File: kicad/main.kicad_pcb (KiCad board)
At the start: 2 copper layers, 198.1 x 99.1 mm, 64 parts, among them J1 Jack-DC, J12 I2C1, J14 LCD_Conn, J15 VIA_A, J2 UART, J3 Data, J4 PWR, J5 uSD, J7 IO~{EN}_{[5..7]}, J8 Control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

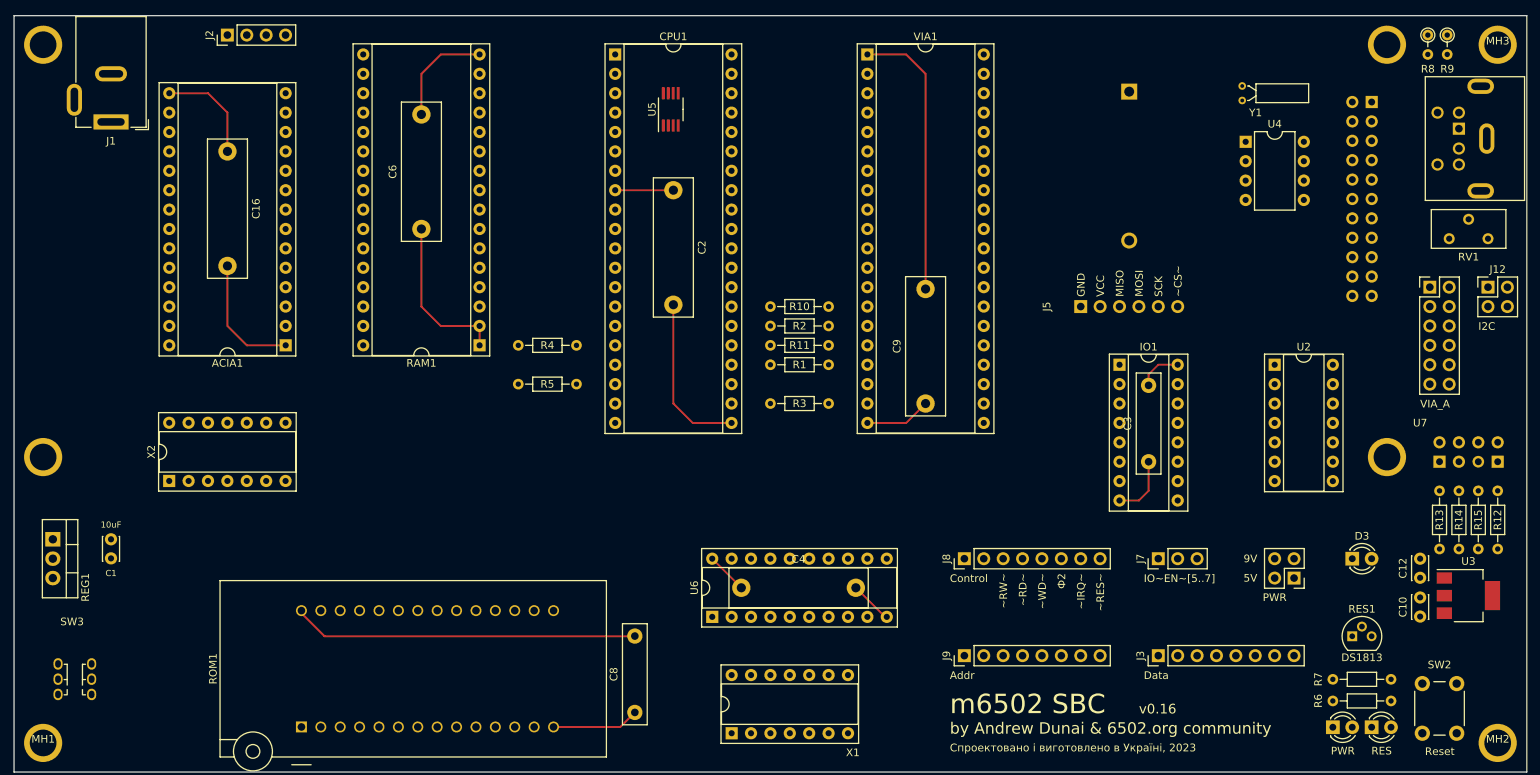
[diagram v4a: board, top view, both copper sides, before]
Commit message: Generate top silk layer with Kicad
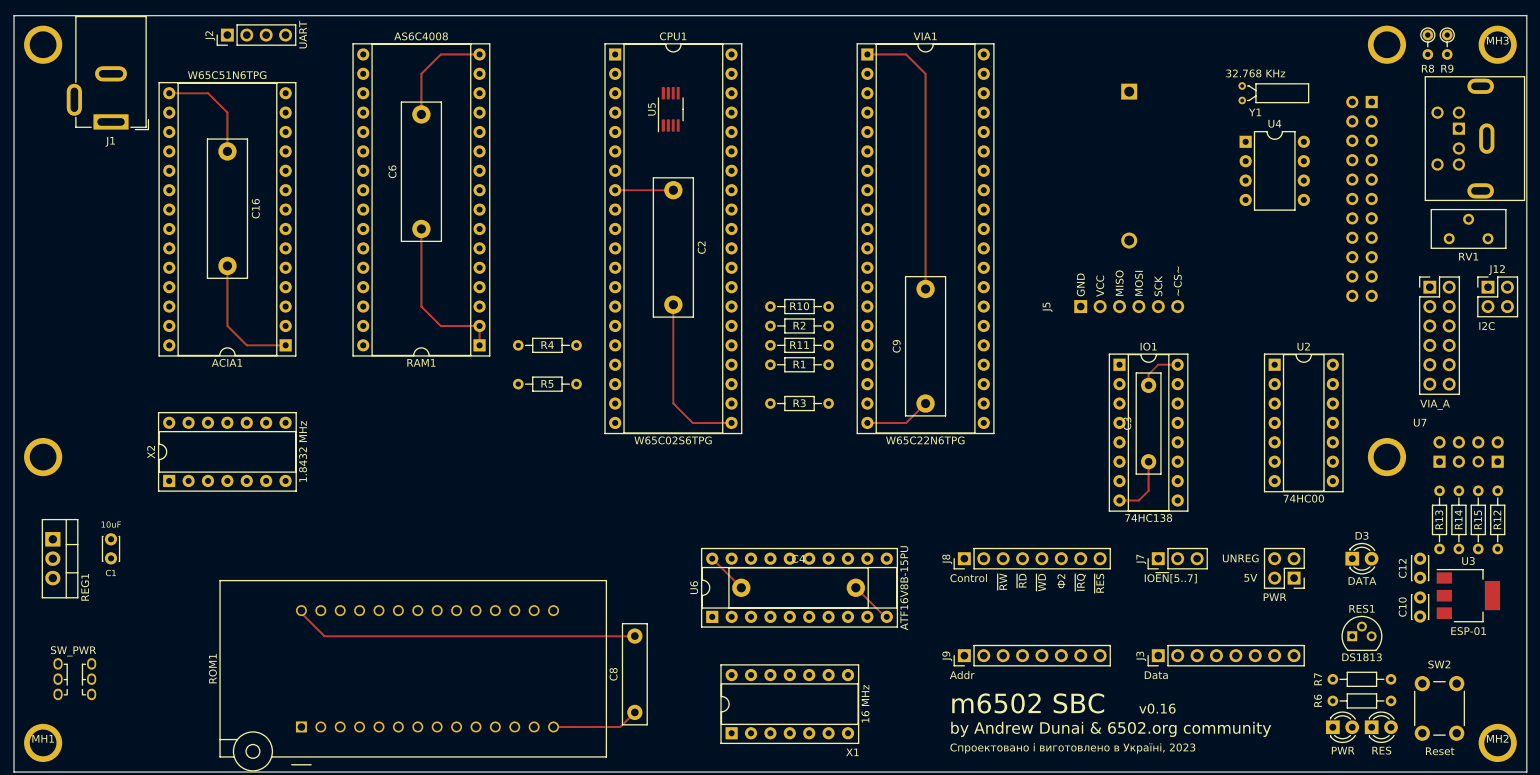
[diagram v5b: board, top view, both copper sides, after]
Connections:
- net +9V renamed +5VA
- net RX renamed ACIARX
- net TX renamed ACIATX
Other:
- board text added: "IO~{EN}[5..7]"
- board text added: "~{IRQ}"
- board text added: "~{RD}"
- board text added: "~{RES}"
- board text added: "~{RW}"
- board text added: "~{WD}"
- board text removed: "IO~EN~[5..7]"
- board text removed: "~IRQ~"
- board text removed: "~RD~"
- board text removed: "~RES~"
- board text removed: "~RW~"
- board text removed: "~WD~"

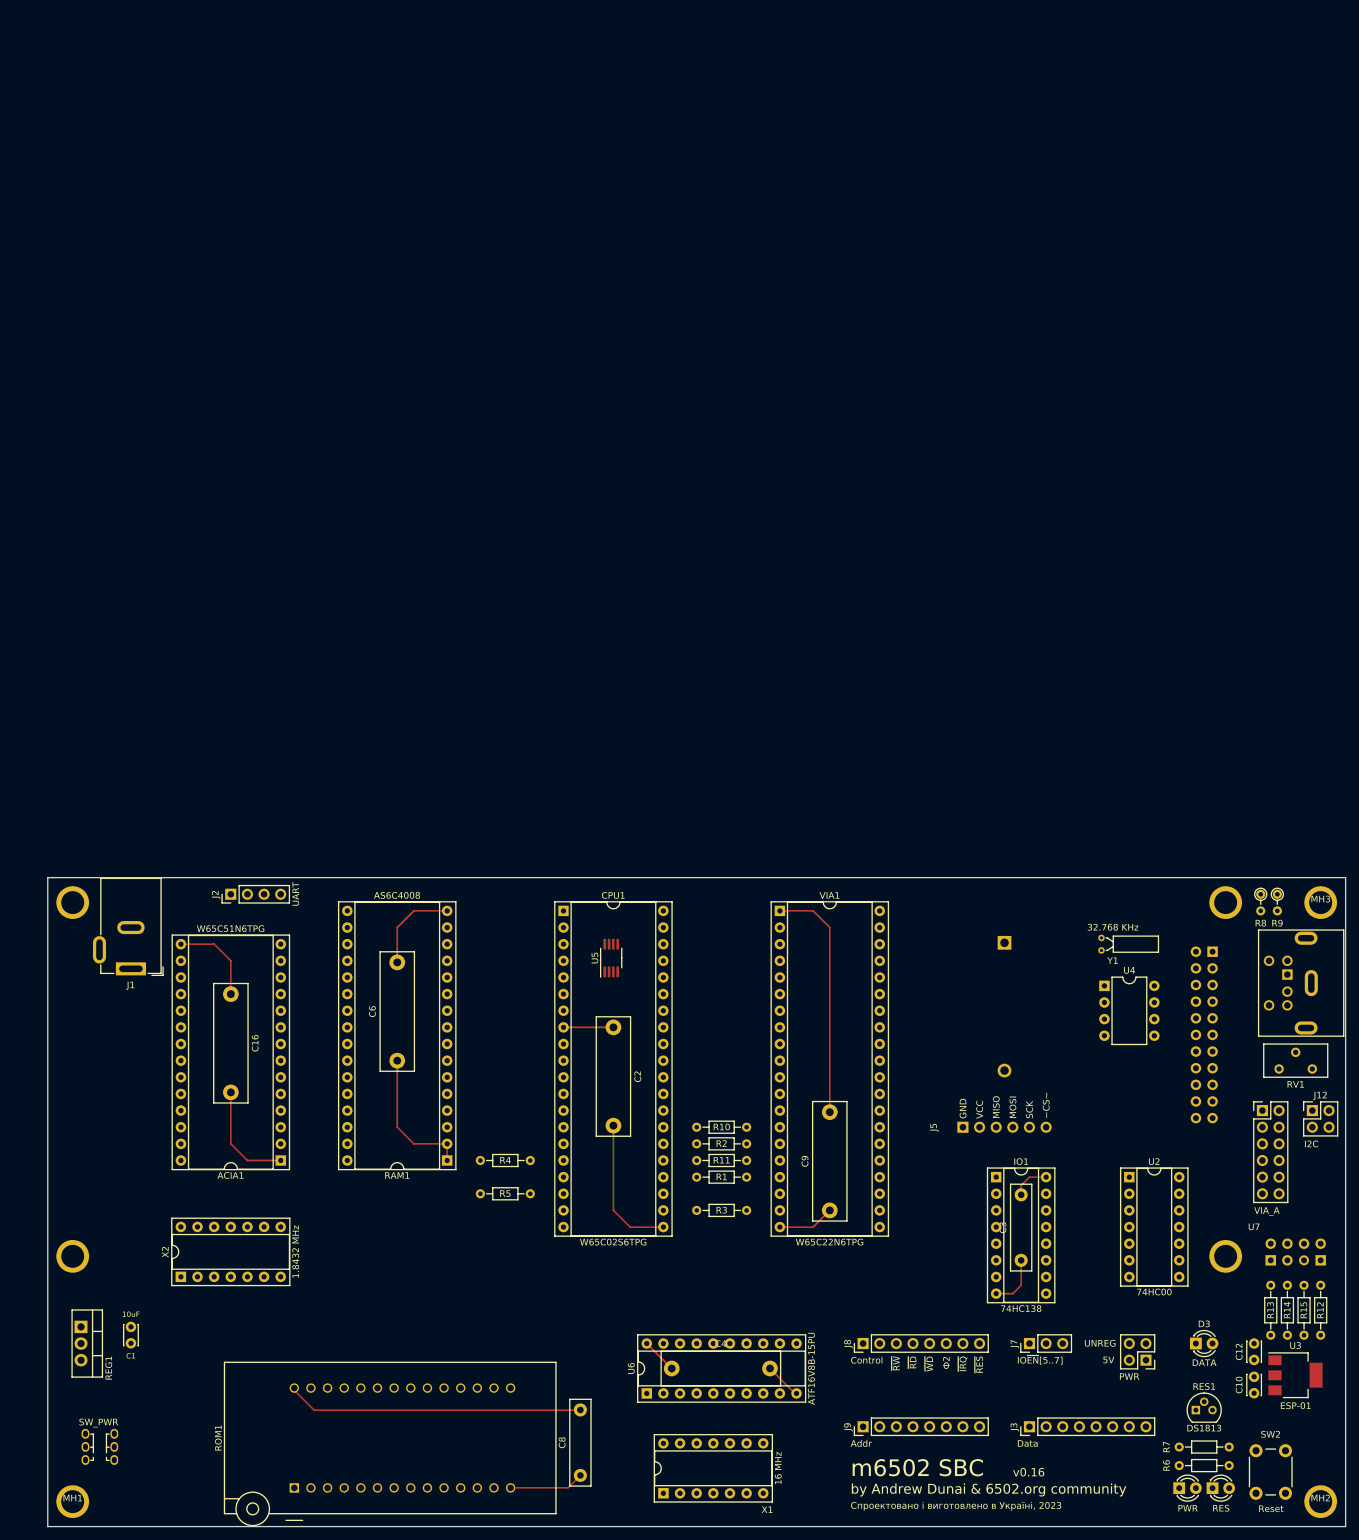
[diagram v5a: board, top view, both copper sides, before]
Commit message: Route /RST to ESP-01
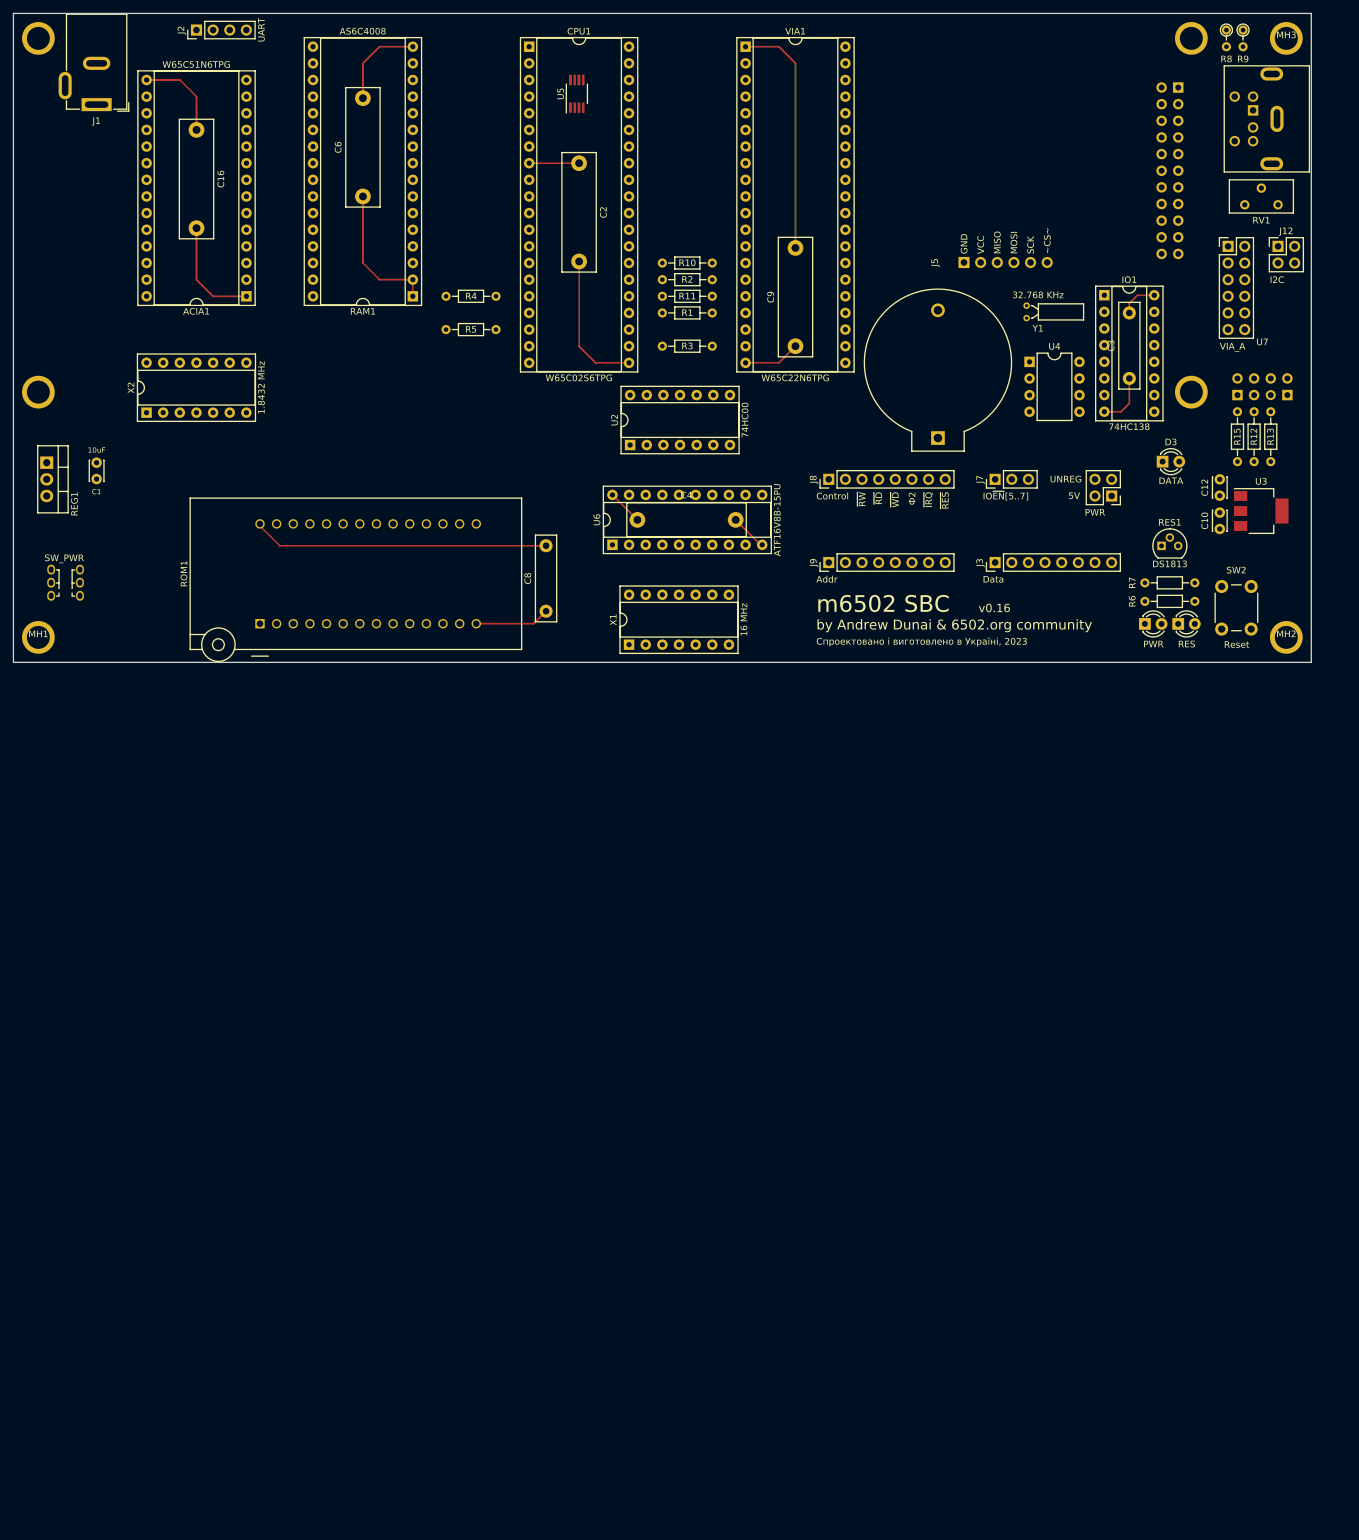
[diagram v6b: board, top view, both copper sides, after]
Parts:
- removed R14: 10K, Resistor_THT:R_Axial_DIN0204_L3.6mm_D1.6mm_P7.62mm_Horizontal
- BT1: moved to F.Cu
- U7: value ESP-01 -> ESP-01-v2
- moved C3 135.6 mm to (180.3, -53.3)
- moved IO1 135.6 mm to (176.5, -66.0)
- moved U2 135.3 mm to (104.1, -43.2), turned to 90 degrees
- moved D3 134.7 mm to (185.4, -40.6)
- moved R12 133.6 mm to (201.9, -40.6)
- moved R13 133.4 mm to (199.4, -48.3)
- moved U7 132.2 mm to (200.7, -54.6)
- moved ACIA1 132.0 mm to (45.6, -65.9)
- moved C10 132.0 mm to (194.2, -30.4)
- moved C12 132.0 mm to (194.2, -35.4)
- moved C16 132.0 mm to (38.0, -91.3)
- moved C2 132.0 mm to (96.3, -86.2)
- moved C6 132.0 mm to (63.4, -81.1)
- moved CPU1 132.0 mm to (88.7, -104.0)
- moved D1 132.0 mm to (182.7, -15.9)
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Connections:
- U7 pad 7: Net-(U7-~{RST}) -> ~{RES}

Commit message: Update silkscreen
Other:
- board text added: "65ad02 SBC"
- board text removed: "m6502 SBC"
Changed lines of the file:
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@@
     (effects (font (size 1 1) (thickness 0.15)) (justify right bottom))
   )
-  (gr_text "m6502 SBC" (at 132.555 -18.89) (layer "F.SilkS")
+  (gr_text "65ad02 SBC" (at 132.555 -18.89) (layer "F.SilkS")
     (effects (font (size 2.54 2.54) (thickness 0.3)) (justify left))
   )

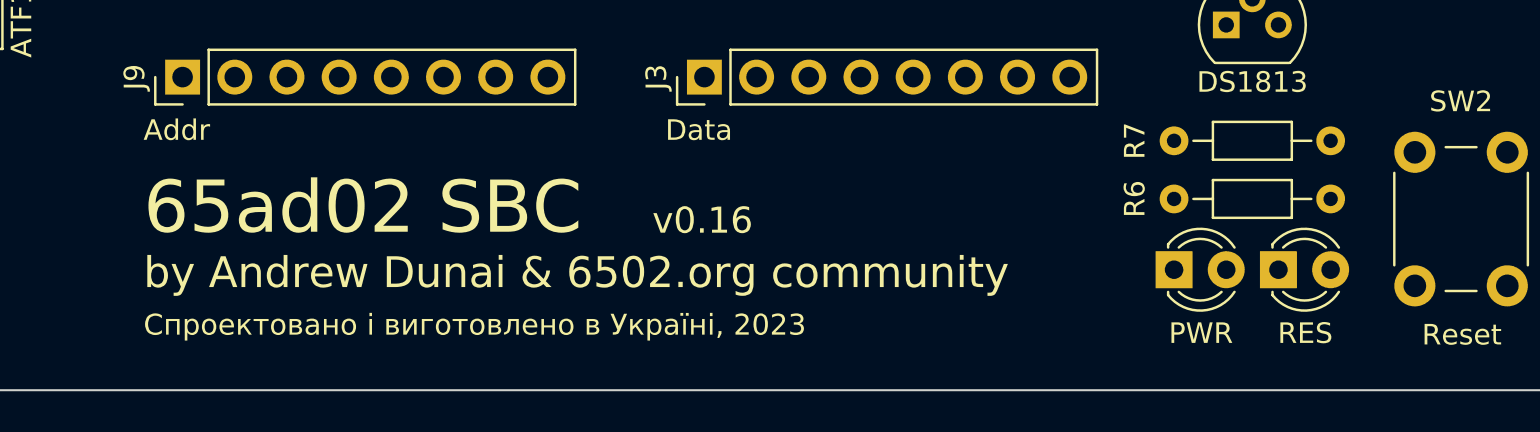
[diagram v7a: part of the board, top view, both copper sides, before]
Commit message: Rename project to Deck65
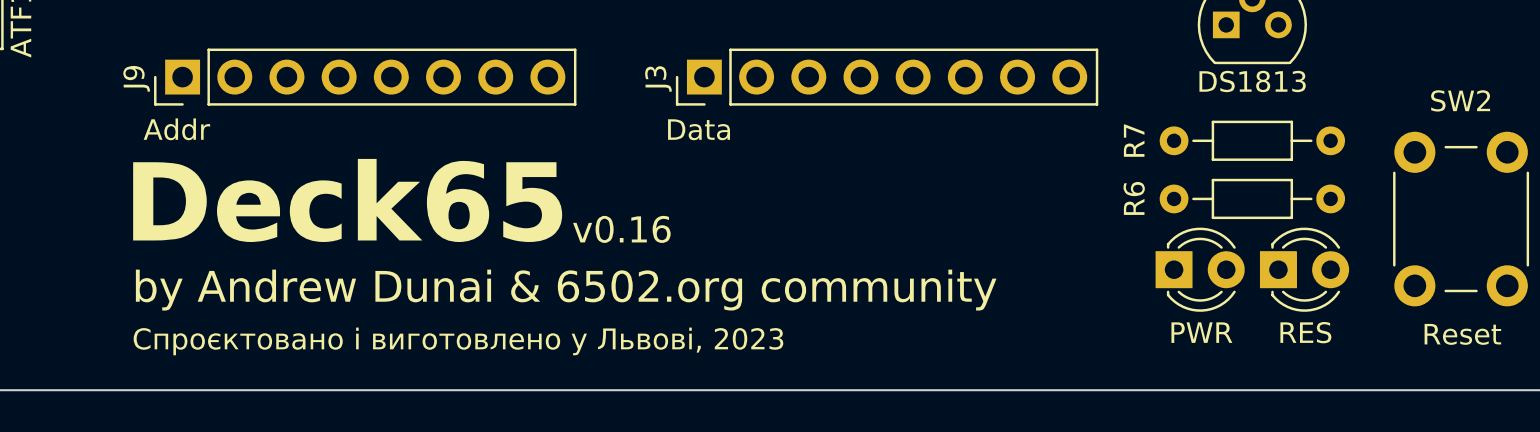
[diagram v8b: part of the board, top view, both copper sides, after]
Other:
- board text added: "Deck65"
- board text added: "Спроєктовано і виготовлено у Львові, 2023"
- board text removed: "65ad02 SBC"
- board text removed: "Спроектовано і виготовлено в Україні, 2023"
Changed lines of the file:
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@@
   (gr_rect (start 10 -109.06) (end 208.12 -10)
     (stroke (width 0.1) (type solid)) (fill none) (layer "Edge.Cuts"))
-  (gr_text "Спроектовано і виготовлено в Україні, 2023" (at 132.555 -13.175) (layer "F.SilkS")
+  (gr_text "Спроєктовано і виготовлено у Львові, 2023" (at 132 -12.46) (layer "F.SilkS")
     (effects (font (size 1.016 1.016) (thickness 0.15875)) (justify left))
   )
@@
     (effects (font (size 1 1) (thickness 0.15)) (justify right bottom))
   )
-  (gr_text "65ad02 SBC" (at 132.555 -18.89) (layer "F.SilkS")
-    (effects (font (size 2.54 2.54) (thickness 0.3)) (justify left))
+  (gr_text "Deck65" (at 131.572 -19.05) (layer "F.SilkS")
+    (effects (font (size 3.81 3.81) (thickness 0.762) bold) (justify left))
   )
   (gr_text "~{IRQ}" (at 150.335 -36.035 90) (layer "F.SilkS")
@@
     (effects (font (size 1 1) (thickness 0.15)))
   )
-  (gr_text "v0.16" (at 157.32 -18.255) (layer "F.SilkS")
+  (gr_text "v0.16" (at 153.416 -17.78) (layer "F.SilkS")
     (effects (font (size 1.27 1.27) (thickness 0.15875)) (justify left))
   )
@@
     (effects (font (size 1 1) (thickness 0.15)) (justify right bottom))
   )
-  (gr_text "by Andrew Dunai & 6502.org community" (at 132.555 -15.715) (layer "F.SilkS")
+  (gr_text "by Andrew Dunai & 6502.org community" (at 132 -15) (layer "F.SilkS")
     (effects (font (size 1.5 1.5) (thickness 0.3)) (justify left))
   )
